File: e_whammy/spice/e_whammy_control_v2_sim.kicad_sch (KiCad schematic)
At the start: 19 parts, among them U1 ${SIM.PARAMS}, U2 ${SIM.PARAMS}, U3 ${SIM.PARAMS}

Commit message: Updated DC servo schematic for spice simulation
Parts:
- removed D1, D2: D, symbol Simulation_SPICE:D
- removed U3: ${SIM.PARAMS}, symbol Simulation_SPICE:OPAMP
- removed V1: 2.5V, symbol Simulation_SPICE:VDC
- removed V2: 5V, symbol Simulation_SPICE:VDC
- added B2: Touch Sensor, symbol Simulation_SPICE:BSOURCE
- added C3, C5, C6: 100nF, symbol Device:C_Small
- added C4: 1uF, symbol Device:C_Small
- added Q1, Q2, Q3: NMOS, symbol cycfi_spice_library:NMOS
- added R11, R12: 10k, symbol Device:R_Small
- added R13, R14: 100k, symbol Device:R_Small
- added R15, R17: 120k, symbol Device:R_Small
- added R16: 100, symbol Device:R_Small
- added R18: 1k, symbol Device:R_Small
- added unit 2 of U1
- added unit 2 of U2
- added U3, U4, U7, U8: OPEN_COLLECTOR_COMPARATOR, symbol cycfi_spice_library:OPEN_COLLECTOR_COMPARATOR
- added U5, U6: ADG779_SPICE, KS_6_ADI, symbol cycfi_spice_library:ADG779
- added V2, V4: VPULSE, symbol Simulation_SPICE:VPULSE
- C1: value 4.7uF -> 10uF
- R10: value 10k -> 100k
- R5: value 90k -> 120k
- R7: value 190k -> 10k
- R8: value 10k -> 120k
- U1, U2: symbol Simulation_SPICE:OPAMP -> cycfi_spice_library:OPAMP
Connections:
- net 0: now also B2.2 (N-); no longer U1.4 (V-), U2.4 (V-)
- net OFFS: now also R10.1
- net OUT: now also U3.2 (-), U4.1 (+), U5.4; no longer R9.2
- net SENSOR: now also C4.1
- net VREF: now also R14.1, R18.1, U5.6, V2.1; no longer R10.1, R6.1
- net at C1.1, R9.1, U1.2 (-): now also R13.2
- net WH: now reaches R5.1, R6.2
- net WH: now also U3.1 (+)
- net +5V: now reaches R5.2
- net +5V: now also R7.2, R11.2, R12.2, R15.2, U1.3 (V+), U2.3 (V+), U3.3 (VCC), U4.3 (VCC), U5.2 (VDD), U6.2 (VDD), U7.3 (VCC), U8.3 (VCC), V4.1; no longer R8.1
- net WL: now reaches R8.2
- net WL: now also R6.1, U4.2 (-); no longer R7.2
- removed net 5V: U1.3 (V+), U2.3 (V+)
- net CLAMP_OUT: no longer names the net of R10.2
- net CLAMP_OUT: now also R13.1, R18.2; no longer R7.1
- new net GND: C3.2, C5.2, C6.2, Q1.3 (S), Q2.3 (S), Q3.3 (S), R17.1, R8.1, U1.4 (V-), U2.4 (V-), U3.4 (VEE), U4.4 (VEE), U5.3 (GND), U6.3 (GND), U7.4 (VEE), U8.4 (VEE), V2.2, V4.2
- new net HOLD: C6.1, Q1.1 (D), Q2.1 (D), R11.1, U5.1
- new net HP: C4.2, R14.2, U7.2 (-), U8.1 (+)
- new net INTEG_IN: R9.2, U5.5
- new net MWH: R15.1, R16.2, U7.1 (+)
- new net MWL: R16.1, R17.2, U8.2 (-)
- new net NMOVEMENT: C5.1, Q3.2 (G), R12.1, U7.5, U8.5
- new net NTOUCH: B2.1 (N+), Q2.2 (G)
- new net WINDOW: C3.1, Q1.2 (G), R7.1, U3.5, U4.5
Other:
- note added: "1: HOLD 0: RESET"
- note added: "1: Idle 0: Movement detected"
- note added: "1: Inside window 0: Outside window"
- note added: "1: Untouched 0: Touched"
- note added: "A simplified raw Hall sensor source in the pre-gain domain, not the final 5 V output domain. * Resting baseline is 2.175 V. * A large upward bend ramps to 2.425 V and holds briefly. * After release, the signal returns to 2.1825 V, modeling a +7.5 mV spring-hysteresis center shift. * A matching large downward bend ramps to 1.925 V, holds, and returns to 2.1675 V before vibrato begins. * After a sh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"
- moved on the sheet: B1, C1, R1, R2, R3, R4, R9

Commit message: Not quite working. WIP. the OUT is falling outside the window
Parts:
- removed C4: 1uF, symbol Device:C_Small
- removed C5: 100nF, symbol Device:C_Small
- removed Q1, Q2, Q3: NMOS, symbol cycfi_spice_library:NMOS
- removed R12: 10k, symbol Device:R_Small
- removed R14: 100k, symbol Device:R_Small
- removed R15, R17: 120k, symbol Device:R_Small
- removed R16: 100, symbol Device:R_Small
- removed U7, U8: OPEN_COLLECTOR_COMPARATOR, symbol cycfi_spice_library:OPEN_COLLECTOR_COMPARATOR
- added U10, U9: OPEN_DRAIN_INVERTER, symbol cycfi_spice_library:OPEN_DRAIN_INVERTER
- U5, U6: value ADG779_SPICE -> ADG779
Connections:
- net +5V: now also U10.3 (VCC), U9.3 (VCC)
- net GND: now also U10.4 (GND), U9.4 (GND)
- net HOLD: now also U10.2, U9.2
- net NTOUCH: now also U9.1
- net WINDOW: now also U10.1
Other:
- note removed: "1: Idle 0: Movement detected"
- moved on the sheet: B1, C3, R5, R6, R7, R8, U1A, U1B, U2B, U3A, U3B, U4A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

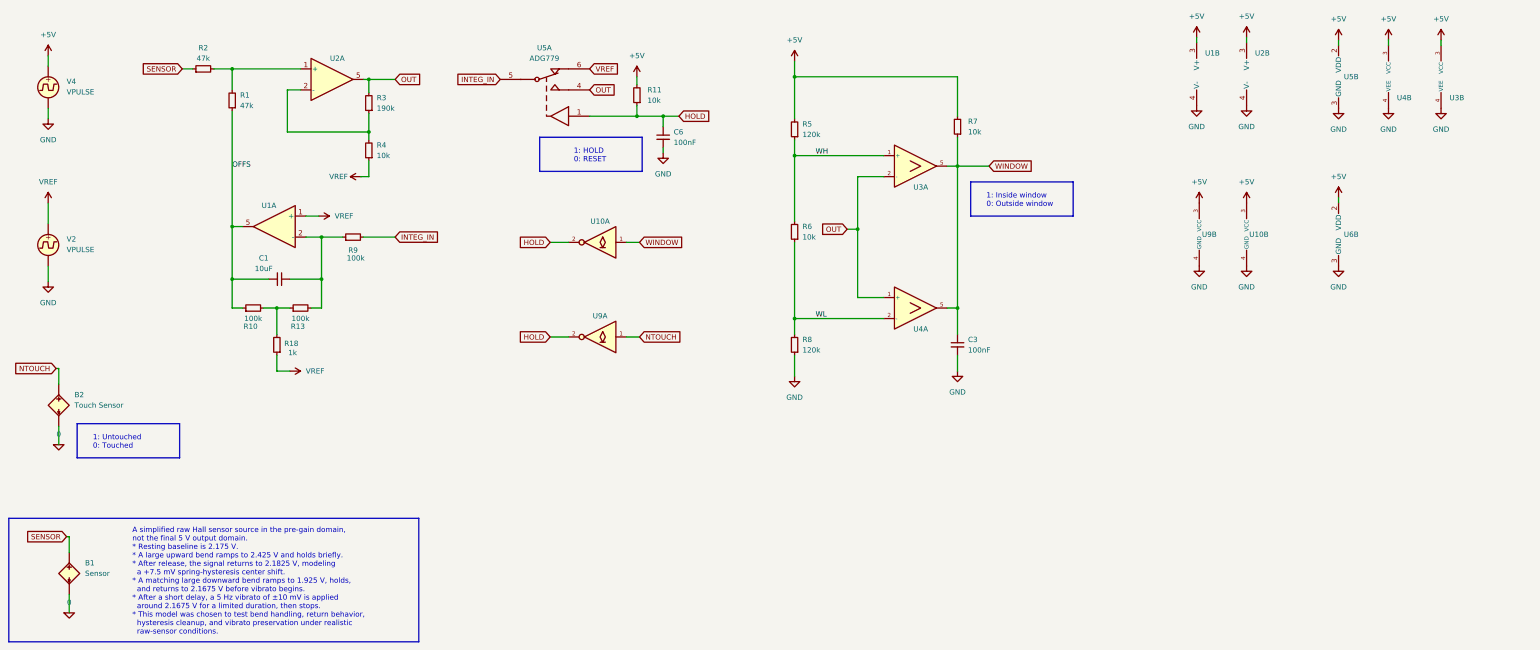
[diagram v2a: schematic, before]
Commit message: Document current e-whammy reset simulation
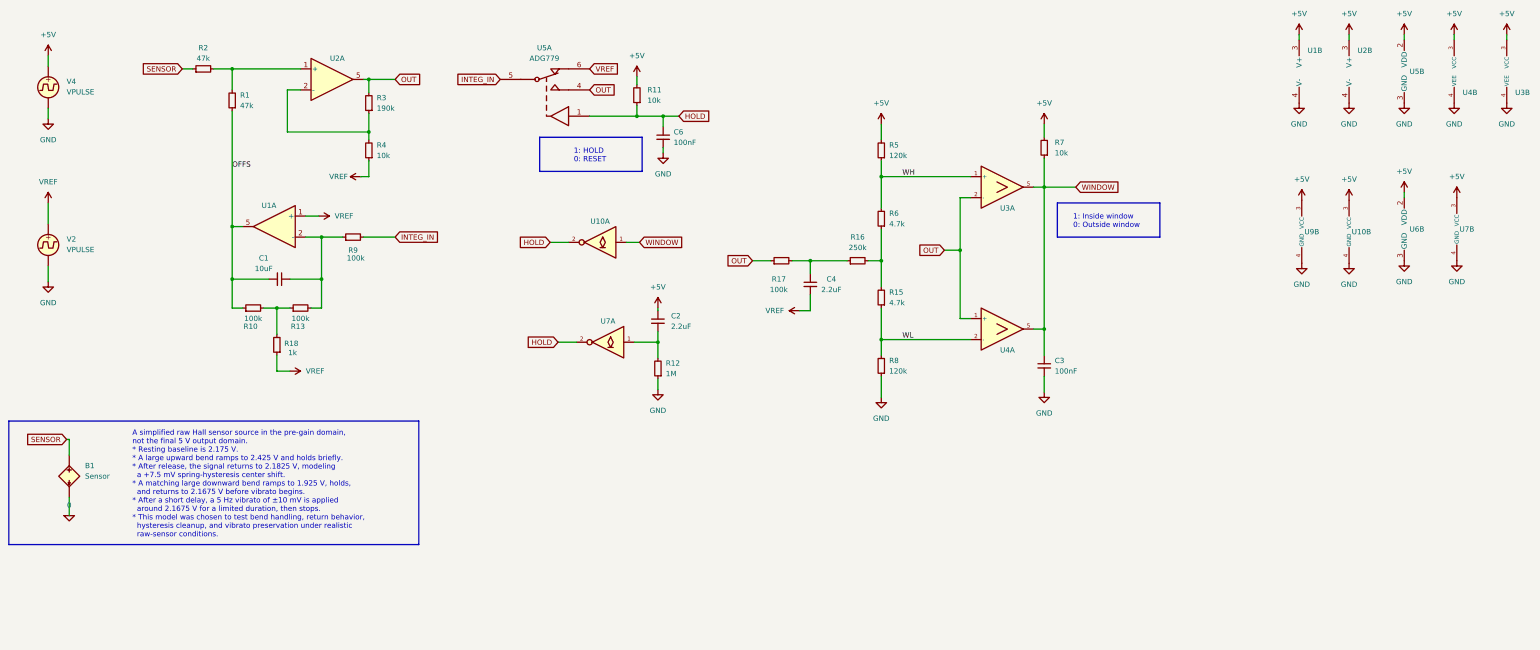
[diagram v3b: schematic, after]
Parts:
- removed B2: Touch Sensor, symbol Simulation_SPICE:BSOURCE
- removed unit 1 of U9
- added C2, C4: 2.2uF, symbol Device:C_Small
- added R12: 1M, symbol Device:R_Small
- added R15: 4.7k, symbol Device:R_Small
- added R16: 250k, symbol Device:R_Small
- added R17: 100k, symbol Device:R_Small
- added U7: OPEN_DRAIN_INVERTER, symbol cycfi_spice_library:OPEN_DRAIN_INVERTER
- R6: value 10k -> 4.7k
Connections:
- net +5V: now also C2.1, U7.3 (VCC)
- net GND: now also R12.1, U7.4 (GND)
- net HOLD: now also U7.2
- net OUT: now also R17.1
- net VREF: now also C4.2
- net WL: now also R15.1; no longer R6.1
- new net: R15.2, R16.2, R6.1
- new net: C2.2, R12.2, U7.1
- new net: C4.1, R16.1, R17.2
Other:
- note removed: "1: Untouched 0: Touched"
- moved on the sheet: B1, C3, R5, R6, R7, R8, U10B, U1B, U2B, U3A, U3B, U4A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

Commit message: Tune e-whammy semitone hold simulation
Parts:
- R18: value 1k -> 499R
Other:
- note added: "A simplified raw Hall sensor source in the pre-gain domain, not the final 5 V output domain. * Resting baseline is 2.175 V. * A large upward bend ramps to 2.425 V and holds briefly. * After release, the signal returns to 2.1825 V, modeling a +7.5 mV spring-hysteresis center shift. * A matching large downward bend ramps to 1.925 V, holds, and returns to 2.1675 V. * Pitch range is now treated as ±1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"
- note added: "Near center reset"
- note added: "Startup reset"
- note removed: "A simplified raw Hall sensor source in the pre-gain domain, not the final 5 V output domain. * Resting baseline is 2.175 V. * A large upward bend ramps to 2.425 V and holds briefly. * After release, the signal returns to 2.1825 V, modeling a +7.5 mV spring-hysteresis center shift. * A matching large downward bend ramps to 1.925 V, holds, and returns to 2.1675 V before vibrato begins. * After a sh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"
- moved on the sheet: C2, R12, U7A

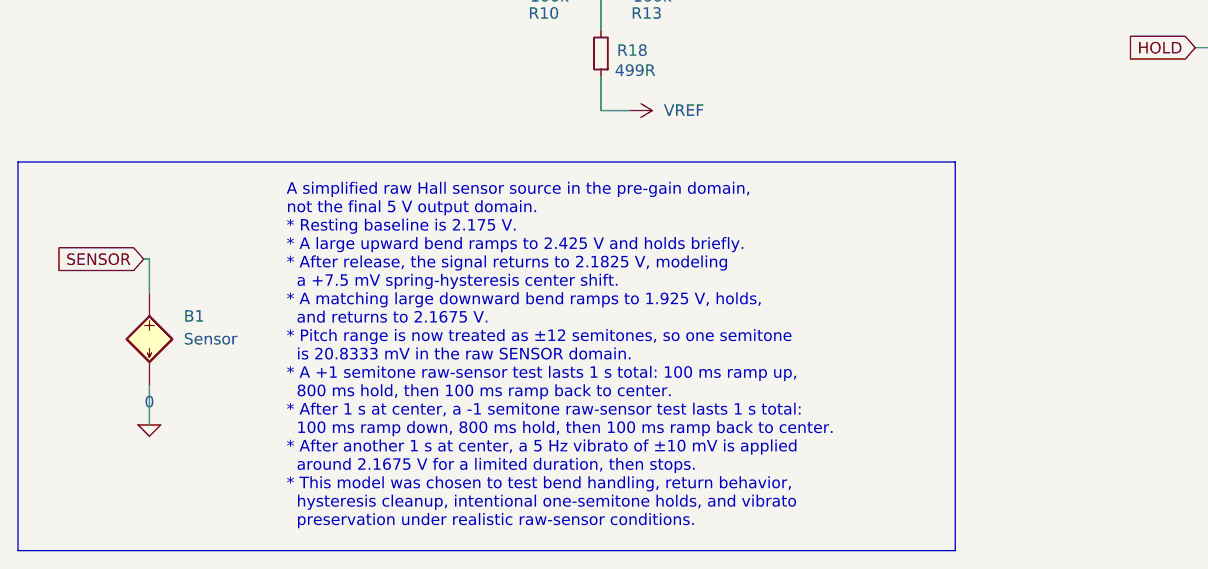
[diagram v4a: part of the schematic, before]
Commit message: Update e-whammy final simulation notes
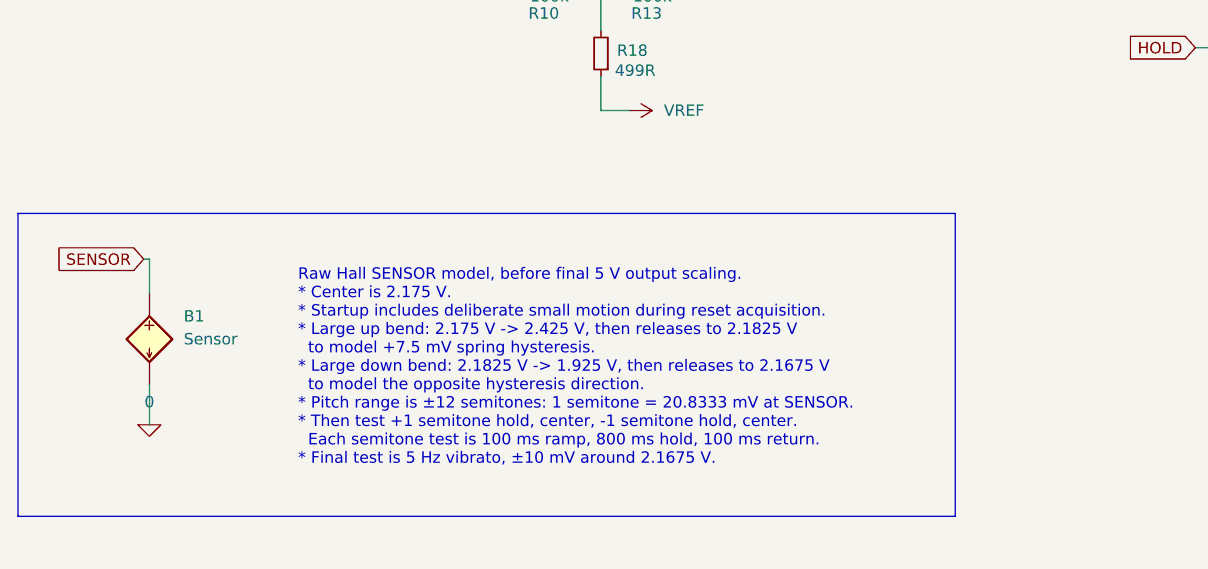
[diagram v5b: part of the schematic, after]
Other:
- note added: "Raw Hall SENSOR model, before final 5 V output scaling. * Center is 2.175 V. * Startup includes deliberate small motion during reset acquisition. * Large up bend: 2.175 V -> 2.425 V, then releases to 2.1825 V to model +7.5 mV spring hysteresis. * Large down bend: 2.1825 V -> 1.925 V, then releases to 2.1675 V to model the opposite hysteresis direction. * Pitch range is ±12 semitones: 1 semitone =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"
- note removed: "A simplified raw Hall sensor source in the pre-gain domain, not the final 5 V output domain. * Resting baseline is 2.175 V. * A large upward bend ramps to 2.425 V and holds briefly. * After release, the signal returns to 2.1825 V, modeling a +7.5 mV spring-hysteresis center shift. * A matching large downward bend ramps to 1.925 V, holds, and returns to 2.1675 V. * Pitch range is now treated as ±1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"
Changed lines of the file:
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@@
 	)
 	(rectangle
-		(start 23.495 129.54)
-		(end 127.635 172.72)
+		(start 23.495 135.255)
+		(end 127.635 168.91)
 		(stroke
 			(width 0)
@@
 		)
 	)
-	(text "A simplified raw Hall sensor source in the pre-gain domain, \nnot the final 5 V output domain.\n* Resting baseline is 2.175 V.\n* A large upward bend ramps to 2.425 V and holds briefly.\n* After release, the signal returns to 2.1825 V, modeling \n  a +7.5 mV spring-hysteresis center shift.\n* A matching large downward bend ramps to 1.925 V, holds, \n  and returns to 2.1675 V.\n* Pitch range is now treated as ±12 semitones, so one semitone \n  is 20.8333 mV in the raw SENSOR domain.\n* A +1 semitone raw-sensor test lasts 1 s total: 100 ms ramp up, \n  800 ms hold, then 100 ms ramp back to center.\n* After 1 s at center, a -1 semitone raw-sensor test lasts 1 s total: \n  100 ms ramp down, 800 ms hold, then 100 ms ramp back to center.\n* After another 1 s at center, a 5 Hz vibrato of ±10 mV is applied \n  around 2.1675 V for a limited duration, then stops.\n* This model was chosen to test bend handling, return behavior, \n  hysteresis cleanup, intentional one-semitone holds, and vibrato \n  preservation under realistic raw-sensor conditions."
+	(text "Raw Hall SENSOR model, before final 5 V output scaling.\n* Center is 2.175 V.\n* Startup includes deliberate small motion during reset acquisition.\n* Large up bend: 2.175 V -> 2.425 V, then releases to 2.1825 V\n  to model +7.5 mV spring hysteresis.\n* Large down bend: 2.1825 V -> 1.925 V, then releases to 2.1675 V\n  to model the opposite hysteresis direction.\n* Pitch range is ±12 semitones: 1 semitone = 20.8333 mV at SENSOR.\n* Then test +1 semitone hold, center, -1 semitone hold, center.\n  Each semitone test is 100 ms ramp, 800 ms hold, 100 ms return.\n* Final test is 5 Hz vibrato, ±10 mV around 2.1675 V."
 		(exclude_from_sim no)
-		(at 53.34 151.13 0)
+		(at 54.61 152.4 0)
 		(effects
 			(font

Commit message: - Cleanup - Simplification
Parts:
- removed C3: 100nF, symbol Device:C_Small
- removed R7: 10k, symbol Device:R_Small
- removed U10, U7, U9: OPEN_DRAIN_INVERTER, symbol cycfi_spice_library:OPEN_DRAIN_INVERTER
- removed U6: ADG779, KS_6_ADI, symbol cycfi_spice_library:ADG779
- added Q1: NMOS, symbol Simulation_SPICE:NMOS
- R4: renamed from R18; value 499R -> 470R
- renumbered C6 to C3, R2 to R1, R11 to R10, R17 to R11, R16 to R12, R5 to R13, R6 to R14, R8 to R16, R1 to R2, R10 to R3, R13 to R5, R9 to R6, R3 to R7, R4 to R8, R12 to R9, U5 to U3, U3 to U4, U3 to U5, U4 to U5, V4 to V1
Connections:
- net +5V: now also R9.2; no longer C2.1
- net GND: now also C2.2; no longer R9.1
- net OUT: now also U3.6; no longer U3.4
- net VREF: now also U3.4; no longer U3.6
- net WINDOW: now also Q1.3 (S)
- net HOLD renamed RESET
- net RESET: now also Q1.1 (D)
- new net: C2.1, Q1.2 (G), R9.1
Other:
- note added: "1: Inside window 0: Outside window Note: Open Drain."
- note added: "1: RESET 0: HOLD"
- note added: "DC Servo"
- note added: "Power Supply"
- note added: "Reset"
- note added: "Reset WIndow Comparator"
- note added: "Sensor Input Simulation"
- note added: "Startup Reset"
- note added: "Threshold Modulation"
- note removed: "1: HOLD 0: RESET"
- note removed: "1: Inside window 0: Outside window"
- note removed: "Near center reset"
- note removed: "Startup reset"
- moved on the sheet: B1, C1, C2, C3, C4, R1, R10, R11, R12, R13, R14, R15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

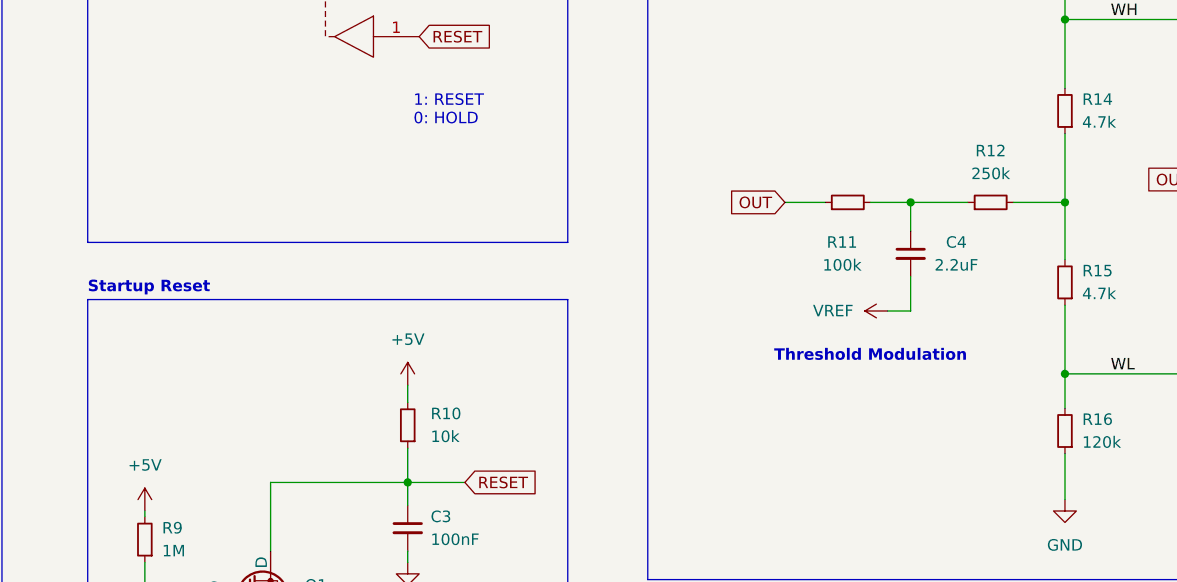
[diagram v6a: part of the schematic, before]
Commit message: Updates using DC servo mechanism
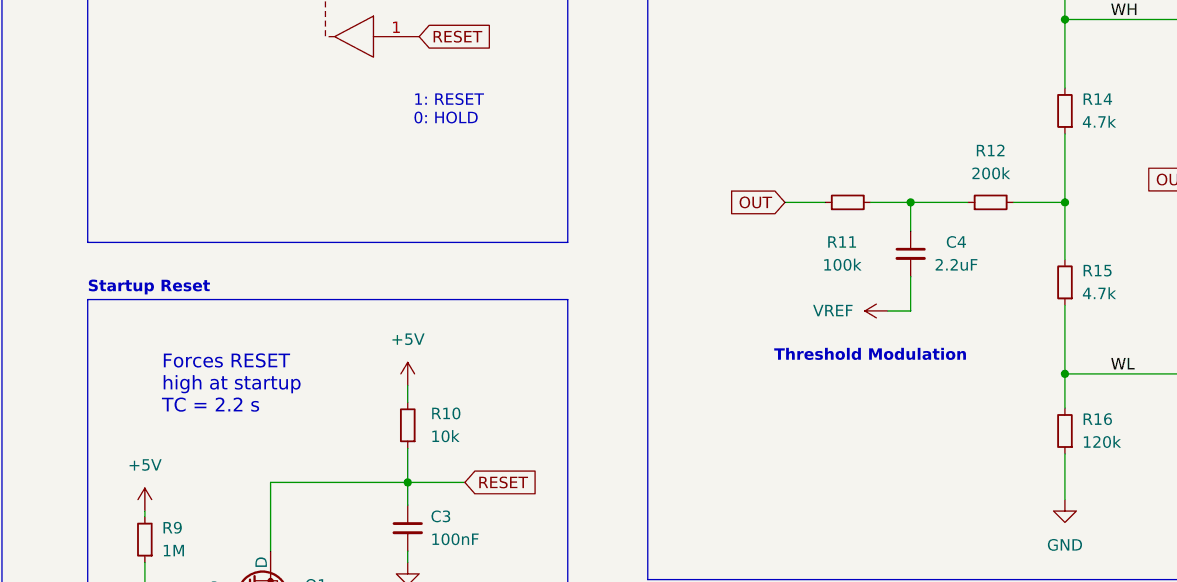
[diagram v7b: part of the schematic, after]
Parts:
- R12: value 250k -> 200k
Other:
- note added: "Forces RESET high at startup TC = 2.2 s"
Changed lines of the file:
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@@
 		)
 	)
+	(text "Forces RESET\nhigh at startup\nTC = 2.2 s"
+		(exclude_from_sim no)
+		(at 181.61 100.33 0)
+		(effects
+			(font
+				(size 1.524 1.524)
+				(thickness 0.1905)
+			)
+			(justify left)
+		)
+	)
 	(text "DC Servo"
 		(exclude_from_sim no)
@@
 			)
 		)
-		(property "Value" "250k"
+		(property "Value" "200k"
 			(at 273.685 76.835 90)
 			(effects
